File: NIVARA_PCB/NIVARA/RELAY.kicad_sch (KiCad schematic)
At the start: 8 parts, among them Q1 PMBT3904, Q2 PMBT3904

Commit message: se agrego diodo de proteccion a los relays
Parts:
- added D1, D2: 1N4007, Diode_SMD:D_SOD-123F, symbol PCM_Diode_AKL:1N4007
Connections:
- net VCC: now also D1.1 (K), D2.1 (K)
- net at Q2.3 (C), RLY2.4: now also D2.2 (A)
- net at Q1.3 (C), RLY1.4: now also D1.2 (A)

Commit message: se agregaron partnumbers
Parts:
- RLY1, RLY2: PART NUMBERT (none) -> SRD-24VDC-SL-C
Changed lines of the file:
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@@
 			)
 		)
-		(property "PART NUMBERT" ""
+		(property "PART NUMBERT" "SRD-24VDC-SL-C"
 			(at 81.28 106.68 0)
 			(effects
@@
 					(size 1.27 1.27)
 				)
+				(hide yes)
 			)
 		)
@@
 			)
 		)
-		(property "PART NUMBERT" ""
+		(property "PART NUMBERT" "SRD-24VDC-SL-C"
 			(at 152.4 111.76 0)
 			(effects
@@
 					(size 1.27 1.27)
 				)
+				(hide yes)
 			)
 		)

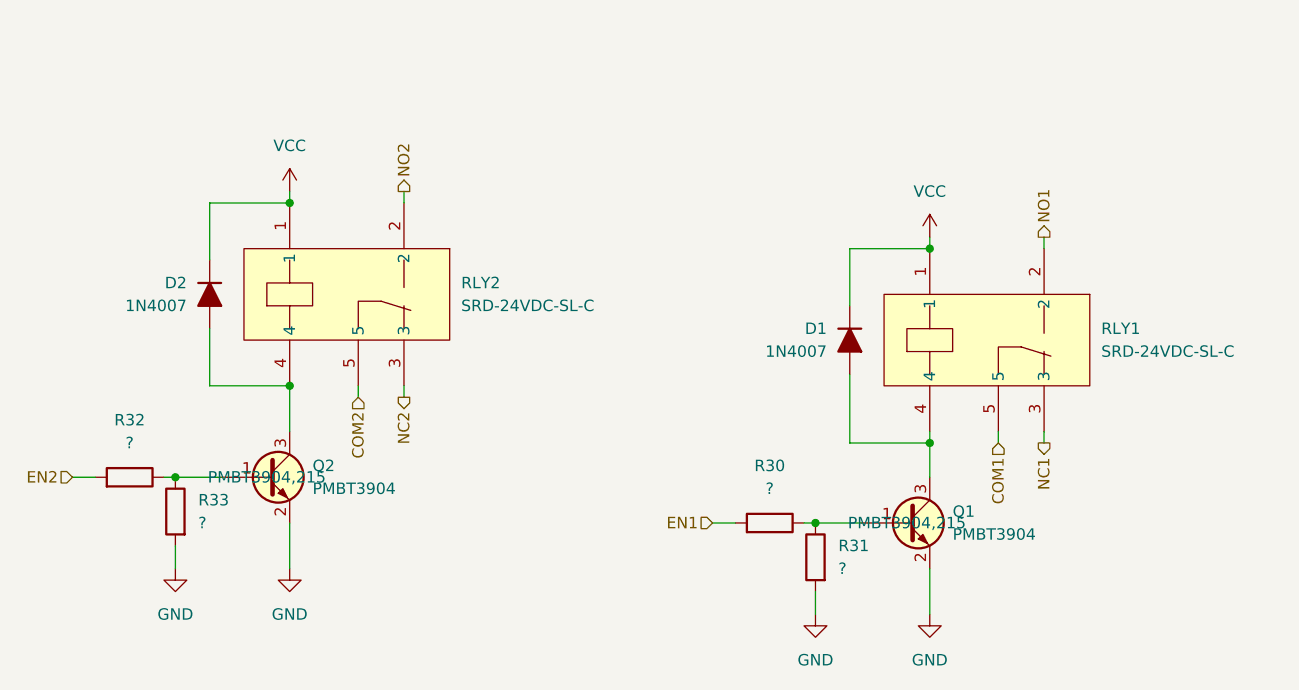
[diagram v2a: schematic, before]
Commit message: RS_485 ADD MODULE
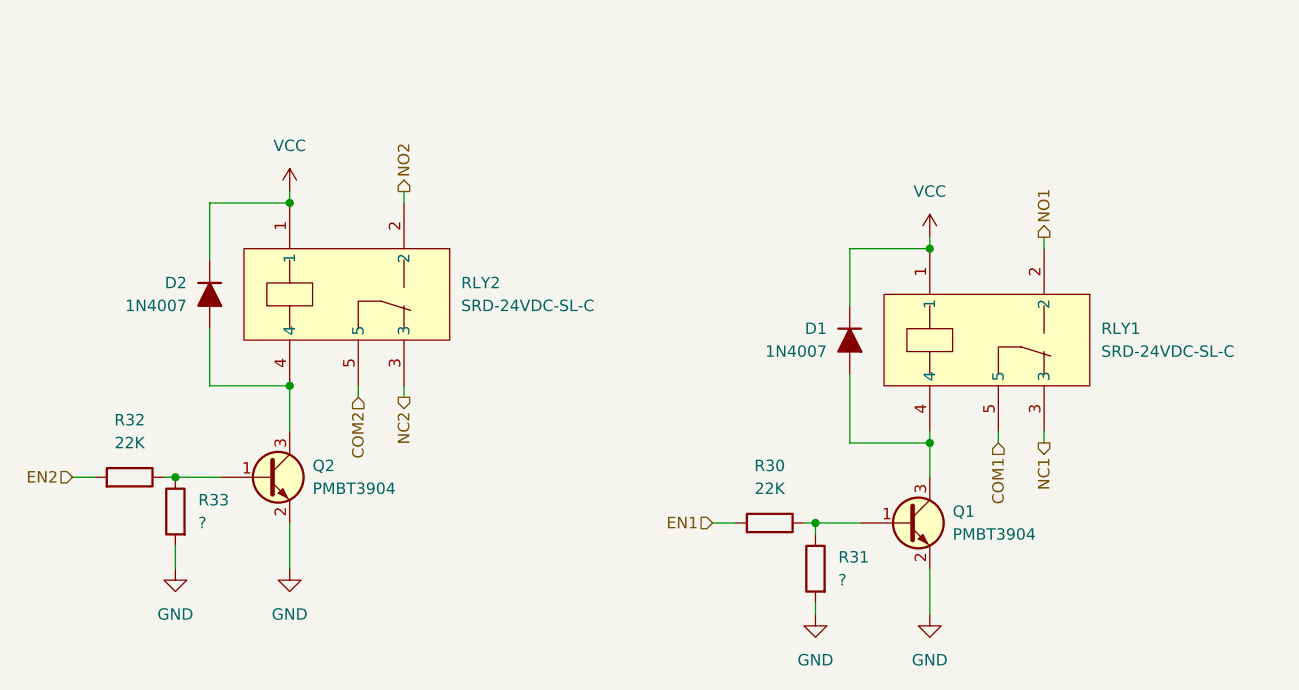
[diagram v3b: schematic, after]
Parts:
- R30, R32: value ? -> 22K; PART NUMBERT (none) -> RC0603FR-0722KL
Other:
- moved on the sheet: R31
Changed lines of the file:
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@@
+	(wire
+		(pts
+			(xy 133.35 133.35) (xy 133.35 132.08)
+		)
+		(stroke
+			(width 0)
+			(type default)
+		)
+	)
 	(wire
 		(pts
@@
 	(wire
 		(pts
-			(xy 133.35 142.24) (xy 133.35 139.7)
+			(xy 133.35 142.24) (xy 133.35 140.97)
 		)
 		(stroke
@@
 	(symbol
 		(lib_id "PCM_Resistor_AKL:R_0603")
-		(at 133.35 135.89 180)
+		(at 133.35 137.16 180)
 		(unit 1)
 		(exclude_from_sim no)
@@
 		(fields_autoplaced yes)
 		(property "Reference" "R31"
-			(at 135.89 134.6199 0)
+			(at 135.89 135.8899 0)
 			(effects
 				(font
@@
 		)
 		(property "Value" "?"
-			(at 135.89 137.1599 0)
+			(at 135.89 138.4299 0)
 			(effects
 				(font
@@
 		)
 		(property "Footprint" "PCM_Resistor_SMD_AKL:R_0603_1608Metric"
-			(at 133.35 124.46 0)
+			(at 133.35 125.73 0)
 			(effects
 				(font
@@
 		)
 		(property "Datasheet" "~"
-			(at 133.35 135.89 0)
+			(at 133.35 137.16 0)
 			(effects
 				(font
@@
 		)
 		(property "Description" "SMD 0603 Chip Resistor, European Symbol, Alternate KiCad Library"
-			(at 133.35 135.89 0)
+			(at 133.35 137.16 0)
 			(effects
 				(font
@@
 		)
 		(property "PART NUMBERT" ""
-			(at 133.35 135.89 0)
+			(at 133.35 137.16 0)
 			(effects
 				(font
@@
 			)
 		)
-		(property "Value" "?"
+		(property "Value" "22K"
 			(at 128.27 128.27 90)
 			(effects
@@
 			)
 		)
-		(property "PART NUMBERT" ""
+		(property "PART NUMBERT" "RC0603FR-0722KL"
 			(at 128.27 132.08 0)
 			(effects
@@
 					(size 1.27 1.27)
 				)
+				(hide yes)
 			)
 		)
@@
 					(size 1.27 1.27)
 				)
+				(hide yes)
 			)
 		)
@@
 			)
 		)
-		(property "Value" "?"
+		(property "Value" "22K"
 			(at 57.15 123.19 90)
 			(effects
@@
 			)
 		)
-		(property "PART NUMBERT" ""
+		(property "PART NUMBERT" "RC0603FR-0722KL"
 			(at 57.15 127 0)
 			(effects
@@
 					(size 1.27 1.27)
 				)
+				(hide yes)
 			)
 		)
@@
 					(size 1.27 1.27)
 				)
-			)
-		)
+				(hide yes)
+			)
+		)

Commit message: Se organizaron componentes en el area de PCB
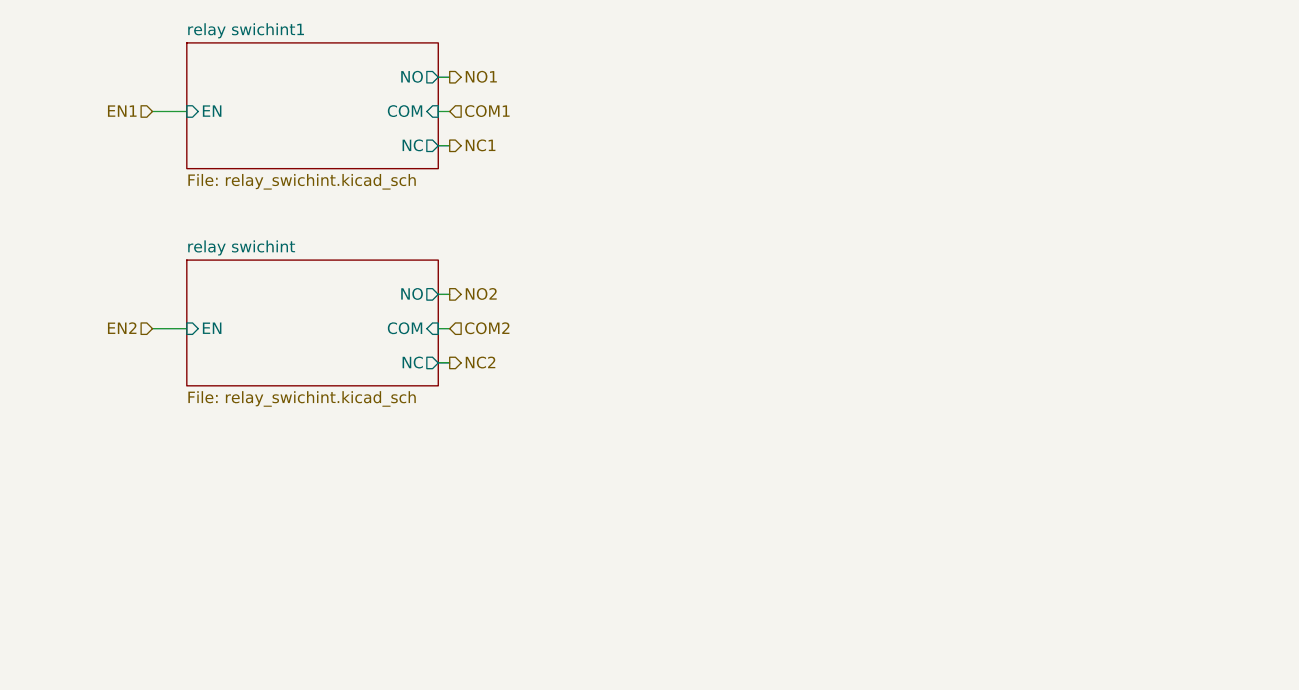
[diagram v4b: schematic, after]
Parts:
- removed D1, D2: 1N4007, Diode_SMD:D_SOD-123F, symbol PCM_Diode_AKL:1N4007
- removed Q1, Q2: PMBT3904, PCM_Package_TO_SOT_SMD_AKL:SOT-23, symbol PCM_Transistor_BJT_AKL:PMBT3904
- removed R30, R32: 22K, PCM_Resistor_SMD_AKL:R_0603_1608Metric, symbol PCM_Resistor_AKL:R_0603
- removed R31, R33: ?, PCM_Resistor_SMD_AKL:R_0603_1608Metric, symbol PCM_Resistor_AKL:R_0603
- removed RLY1, RLY2: SRD-24VDC-SL-C, easyeda2kicad:RELAY-TH_SRD-XXVDC-XL-C, symbol easyeda2kicad:SRD-24VDC-SL-C
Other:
- added sheet relay swichint (relay_swichint.kicad_sch)
- added sheet relay swichint1 (relay_swichint.kicad_sch)
